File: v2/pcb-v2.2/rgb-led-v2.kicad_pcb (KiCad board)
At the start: 2 copper layers, 90 x 50 mm, 16 parts, among them CON1 BARREL_JACK, SW1 SPST

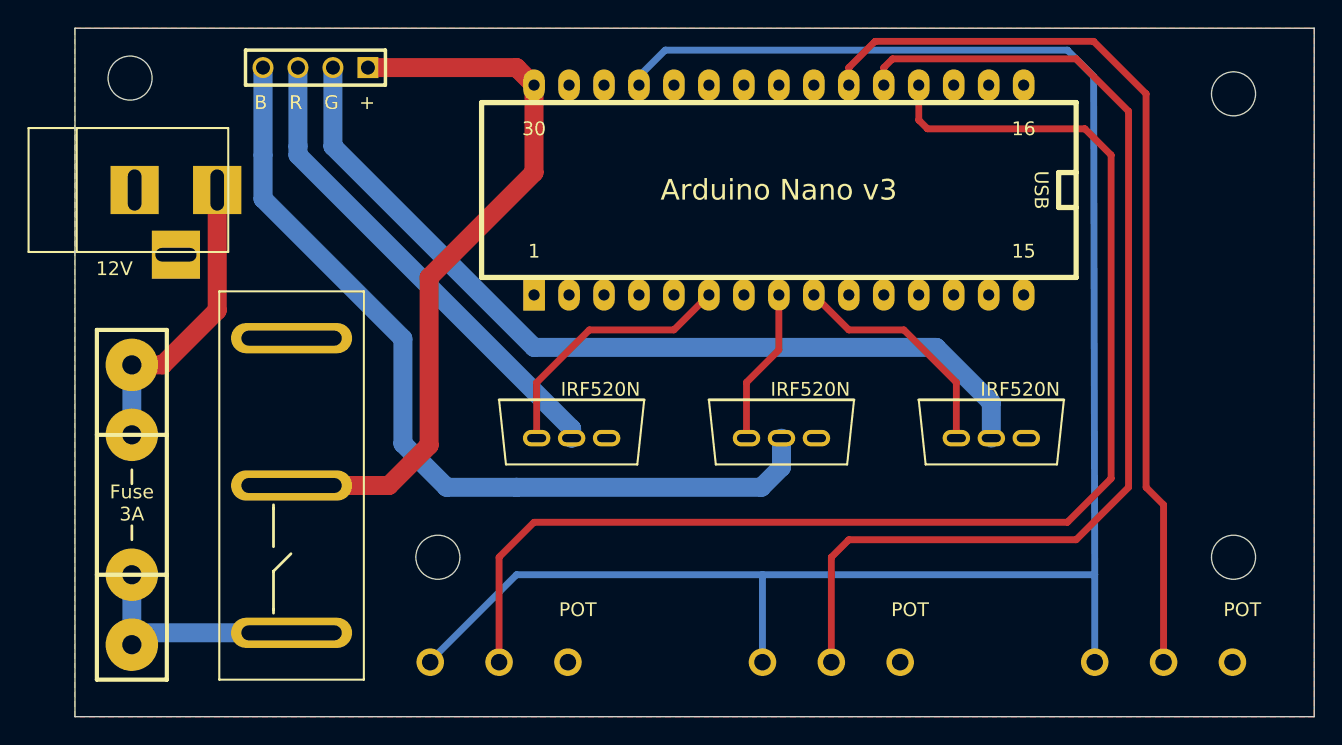
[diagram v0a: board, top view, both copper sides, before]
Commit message: Improved routing, thinner traces
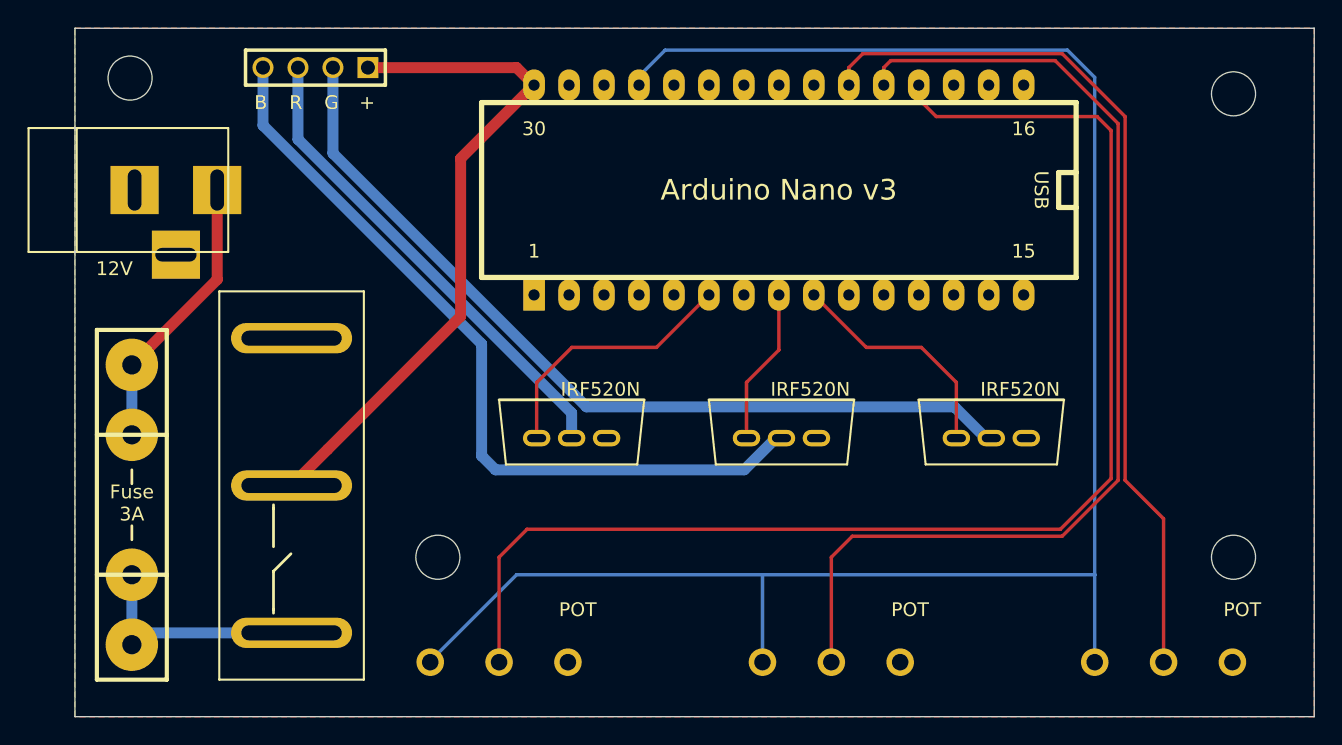
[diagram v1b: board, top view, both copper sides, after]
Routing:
- net Net-(CONN1-Pad4): track 63.1 -> 58.0 mm
- net Net-(CONN1-Pad1): track 53.1 -> 49.0 mm
- net Net-(RV3-Pad2): track 67.0 -> 64.4 mm
- net Net-(RV2-Pad2): track 79.5 -> 77.1 mm
- net Net-(CON1-Pad1): track 21.7 -> 20.3 mm
- net Net-(F1-Pad2): track 15.8 -> 17.0 mm
- net Net-(CONN1-Pad2): track 63.9 -> 62.7 mm
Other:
- net class Default: clearance 0.015 -> 0.15; trace_width 0.01 -> 0.25; via_dia 0.0295 -> 1; via_drill 0.0197 -> 0.8
- net class PWR added: clearance 0.15, trace_width 0.8, via_dia 1, via_drill 0.8
- rule trace_clearance: 0.015 -> 0.15

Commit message: Add pin headers to Arduino
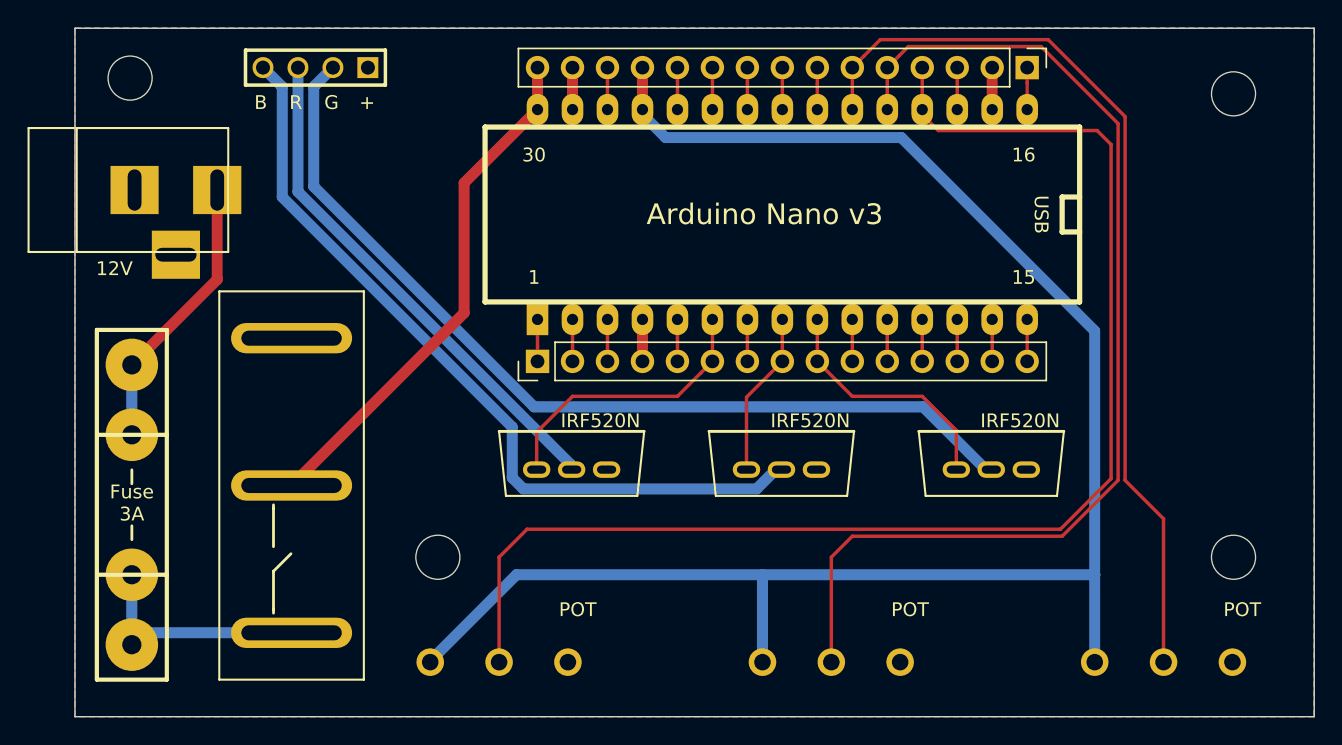
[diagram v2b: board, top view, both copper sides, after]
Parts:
- added P1: CONN_01X15, Pin_Headers:Pin_Header_Straight_1x15_Pitch2.54mm, F.Cu at (87.9, 22.9)
- added P2: CONN_01X15, Pin_Headers:Pin_Header_Straight_1x15_Pitch2.54mm, F.Cu at (52.3, 44.2)
- moved QB1 2.29 mm to (64.8, 49.3)
- moved QG1 2.29 mm to (80.0, 49.3)
- moved QR1 2.29 mm to (49.5, 49.3)
- moved UC1 1.80 mm to (68.8, 33.5)
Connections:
- net Net-(CONN1-Pad1) renamed VIN
- net Net-(QB1-PadG) renamed A23
- net Net-(QG1-PadG) renamed A24
- net Net-(QR1-PadG) renamed A21
- net Net-(RV1-Pad1) renamed 5V
- net Net-(RV1-Pad2) renamed A4
- net Net-(RV2-Pad2) renamed A5
- net Net-(RV3-Pad2) renamed A6
- UC1 pad 1: Net-(UC1-Pad1) -> A1
- UC1 pad 10: Net-(UC1-Pad10) -> A10
- UC1 pad 11: Net-(UC1-Pad11) -> A11
- UC1 pad 13: Net-(UC1-Pad13) -> A13
- UC1 pad 16: Net-(UC1-Pad16) -> A16
- UC1 pad 17: Net-(UC1-Pad17) -> A17
- UC1 pad 18: Net-(UC1-Pad18) -> A18
- UC1 pad 2: Net-(UC1-Pad2) -> 3.3V
- UC1 pad 20: Net-(UC1-Pad20) -> A20
- UC1 pad 22: Net-(UC1-Pad22) -> A22
- UC1 pad 25: Net-(UC1-Pad25) -> A25
- UC1 pad 26: Net-(UC1-Pad26) -> A26
- UC1 pad 27: Net-(UC1-Pad27) -> A27
- UC1 pad 28: Net-(UC1-Pad28) -> A28
- UC1 pad 29: Net-(UC1-Pad29) -> A29
- UC1 pad 3: Net-(UC1-Pad3) -> A3
- UC1 pad 30: Net-(UC1-Pad30) -> A30
- UC1 pad 7: Net-(UC1-Pad7) -> A7
- UC1 pad 8: Net-(UC1-Pad8) -> A8
- UC1 pad 9: Net-(UC1-Pad9) -> A9
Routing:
- net VIN: track 49.0 -> 37.7 mm
- net 5V: track 135.1 -> 124.1 mm
- net GND: track 0.00 -> 6.10 mm
- net Net-(CONN1-Pad2): track 62.7 -> 67.0 mm
- net A9: track 0.00 -> 3.05 mm
- net A8: track 0.00 -> 3.05 mm
- net A7: track 0.00 -> 3.05 mm
- net A3: track 0.00 -> 3.05 mm
- net A13: track 0.00 -> 3.05 mm
- net A11: track 0.00 -> 3.05 mm
- net A10: track 0.00 -> 3.05 mm
- net A1: track 0.00 -> 3.05 mm
- net 3.3V: track 0.00 -> 3.05 mm
- net A30: track 0.00 -> 3.05 mm
- net A29: track 0.00 -> 3.05 mm
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- added copper zone on B.Cu, net GND

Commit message: Add pin headers to PCB
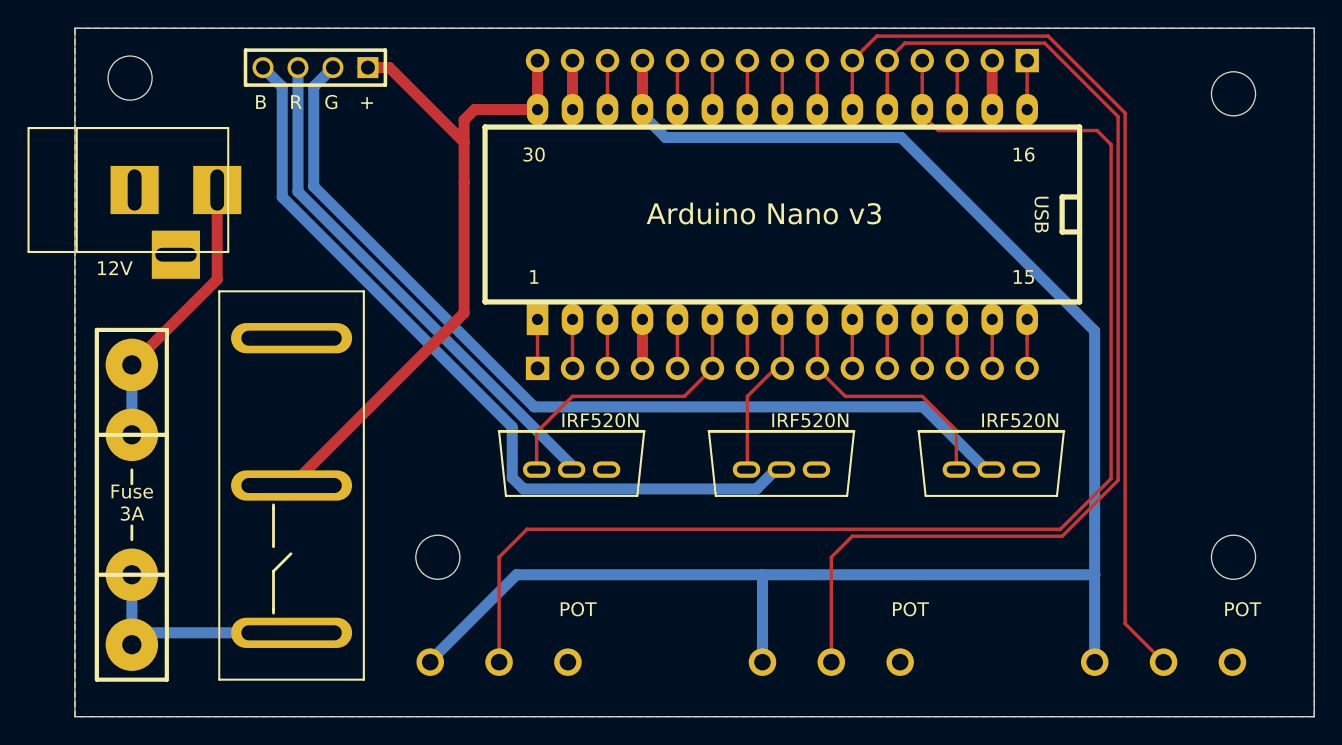
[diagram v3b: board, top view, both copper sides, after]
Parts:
- P1, P2: footprint Pin_Headers:Pin_Header_Straight_1x15_Pitch2.54mm -> rgbled-custom:Pin_Header_Straight_1x15_Pitch2.54mm_Noborder
- moved P2 0.51 mm to (52.3, 44.7)
- moved P1 0.51 mm to (87.9, 22.4)
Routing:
- net VIN: track 37.7 -> 50.2 mm
- net GND: track 6.10 -> 7.11 mm
- net A5: track 79.4 -> 80.2 mm
- net A6: track 66.8 -> 67.5 mm
- net A30: track 3.05 -> 3.56 mm
- net A29: track 3.05 -> 3.56 mm
- net A28: track 3.05 -> 3.56 mm
- net A27: track 3.05 -> 3.56 mm
- net A26: track 3.05 -> 3.56 mm
- net A25: track 3.05 -> 3.56 mm
- net A22: track 3.05 -> 3.56 mm
- net A20: track 3.05 -> 3.56 mm
- net A18: track 3.05 -> 3.56 mm
- net A17: track 3.05 -> 3.56 mm
- net A16: track 3.05 -> 3.56 mm
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
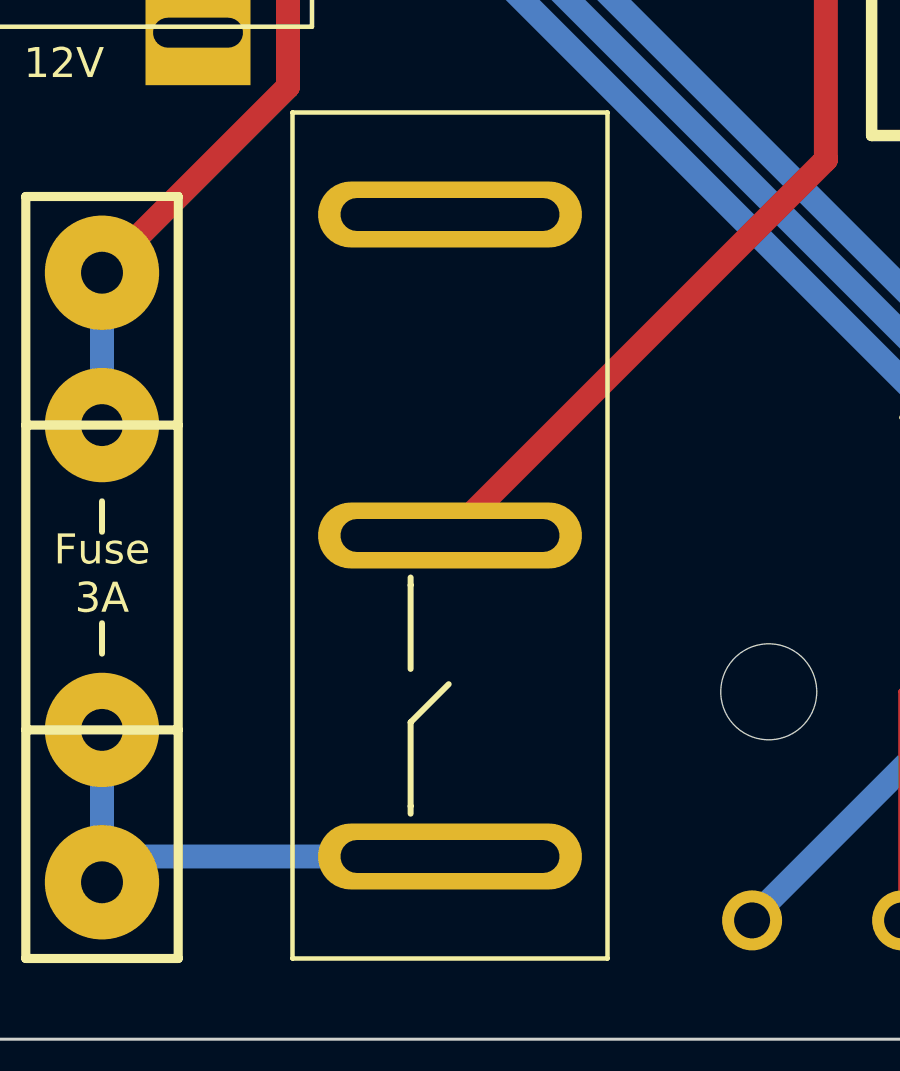
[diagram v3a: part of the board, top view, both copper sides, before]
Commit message: Made switch holes a bit wider again
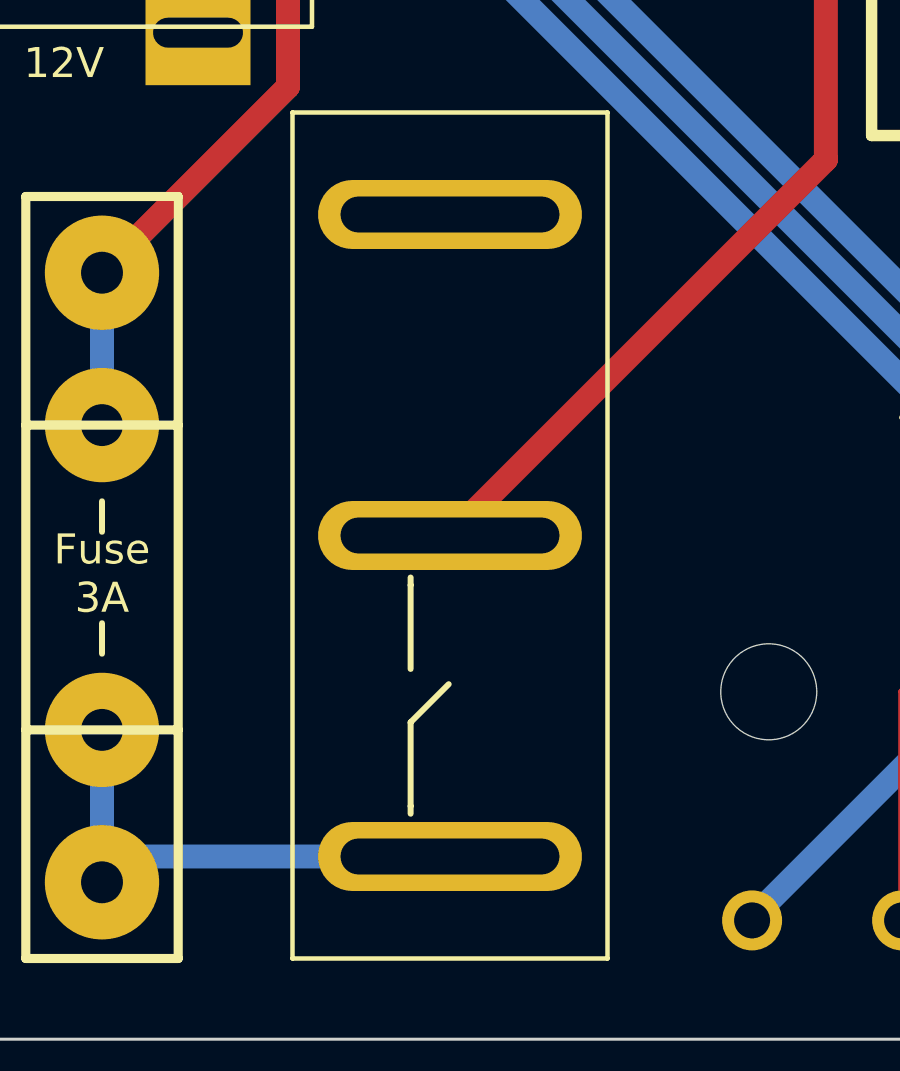
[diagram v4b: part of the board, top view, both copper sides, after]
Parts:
- SW1: footprint KCD3 -> rgbled-custom:KCD3
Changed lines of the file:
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@@
     (add_net VIN)
+  )
+  (module rgbled-custom:KCD3 (layer F.Cu)
+    (at 29.21 67.31 90)
+    (fp_text reference SW1 (at 7.62 5.08 180) (layer F.SilkS) hide
+      (effects (font (size 1 1) (thickness 0.15)))
+    )
+    (fp_text value SPST (at 10.16 5.08 180) (layer F.SilkS) hide
+      (effects (font (size 1 1) (thickness 0.15)))
+    )
+    (fp_line (start 28.2 10.5) (end 0 10.5) (layer F.SilkS) (width 0.15))
+    (fp_line (start 28.2 0) (end 28.2 10.5) (layer F.SilkS) (width 0.15))
+    (fp_line (start 0 0) (end 28.2 0) (layer F.SilkS) (width 0.15))
+    (fp_line (start 0 10.5) (end 0 0) (layer F.SilkS) (width 0.15))
+    (pad 1 thru_hole oval (at 3.4 5.25 90) (size 2.3 8.8) (drill oval 1.2 7.3) (layers *.Cu *.Mask F.SilkS)
+      (net 6 "Net-(F1-Pad2)"))
+    (pad 2 thru_hole oval (at 14.1 5.25 90) (size 2.3 8.8) (drill oval 1.2 7.3) (layers *.Cu *.Mask F.SilkS)
+      (net 8 VIN))
+    (pad 3 thru_hole oval (at 24.8 5.25 90) (size 2.3 8.8) (drill oval 1.2 7.3) (layers *.Cu *.Mask F.SilkS))
   )
   (module arduino_nano (layer F.Cu)
@@
     (pad 1 np_thru_hole circle (at 0 0) (size 3.2 3.2) (drill 3.2) (layers *.Cu *.Mask F.SilkS))
   )
-  (module KCD3 (layer F.Cu)
-    (at 29.21 67.31 90)
-    (fp_text reference SW1 (at 7.62 5.08 180) (layer F.SilkS) hide
-      (effects (font (size 1 1) (thickness 0.15)))
-    )
-    (fp_text value SPST (at 10.16 5.08 180) (layer F.SilkS) hide
-      (effects (font (size 1 1) (thickness 0.15)))
-    )
-    (fp_line (start 28.2 10.5) (end 0 10.5) (layer F.SilkS) (width 0.15))
-    (fp_line (start 28.2 0) (end 28.2 10.5) (layer F.SilkS) (width 0.15))
-    (fp_line (start 0 0) (end 28.2 0) (layer F.SilkS) (width 0.15))
-    (fp_line (start 0 10.5) (end 0 0) (layer F.SilkS) (width 0.15))
-    (pad 1 thru_hole oval (at 3.4 5.25 90) (size 2.2 8.8) (drill oval 1.1 7.3) (layers *.Cu *.Mask F.SilkS)
-      (net 6 "Net-(F1-Pad2)"))
-    (pad 2 thru_hole oval (at 14.1 5.25 90) (size 2.2 8.8) (drill oval 1.1 7.3) (layers *.Cu *.Mask F.SilkS)
-      (net 8 VIN))
-    (pad 3 thru_hole oval (at 24.8 5.25 90) (size 2.2 8.8) (drill oval 1.1 7.3) (layers *.Cu *.Mask F.SilkS))
-  )
   (module POT_3 (layer F.Cu)

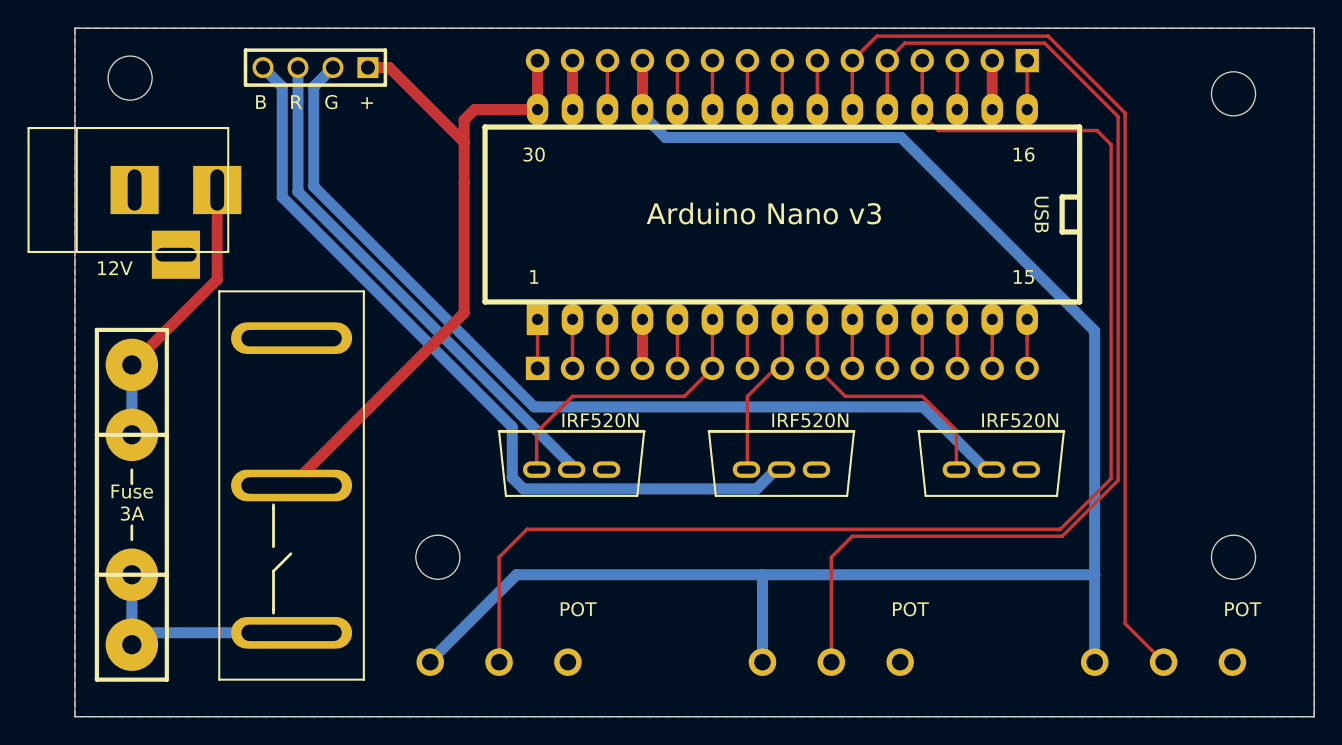
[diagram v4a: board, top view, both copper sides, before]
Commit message: Two push buttons (fixes #2)
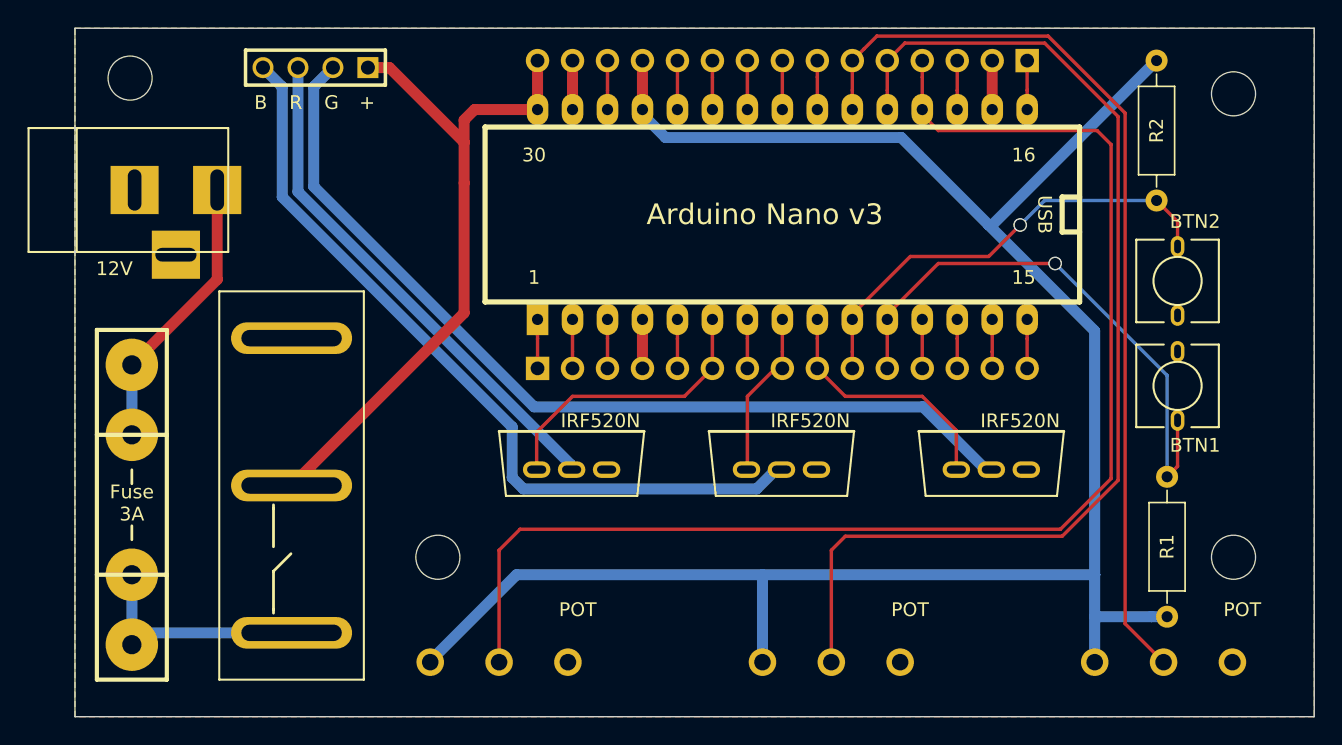
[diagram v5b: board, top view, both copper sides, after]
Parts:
- added BTN1: SPST, rgbled-custom:PUSHBUTTON_TS044S, F.Cu at (98.8, 46.0)
- added BTN2: SPST, rgbled-custom:PUSHBUTTON_TS044S, F.Cu at (98.8, 38.4)
- added R1: R, Resistors_THT:R_Axial_DIN0207_L6.3mm_D2.5mm_P10.16mm_Horizontal, F.Cu at (98.0, 52.6)
- added R2: R, Resistors_THT:R_Axial_DIN0207_L6.3mm_D2.5mm_P10.16mm_Horizontal, F.Cu at (97.3, 32.5)
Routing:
- net A26: track 3.56 -> 40.9 mm, vias 0 -> 1
- net A25: track 3.56 -> 33.4 mm, vias 0 -> 1
- net 5V: track 124.6 -> 147.0 mm
